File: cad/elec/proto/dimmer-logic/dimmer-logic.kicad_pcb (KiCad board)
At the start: 2 copper layers, 41 parts, among them P1 AC_IN, P2 DC_OUT, P3 LOGIC_OUT, P4 I2C_BUS, P5 dsPIC_PGM, U1 7805, U2 LTC6253, U3 TCA9406, U4 dsPIC33FJ06GS101A, U5 74LS08, U6 74LS32, U7 MIC52393.3-YS, X1 10 MHz

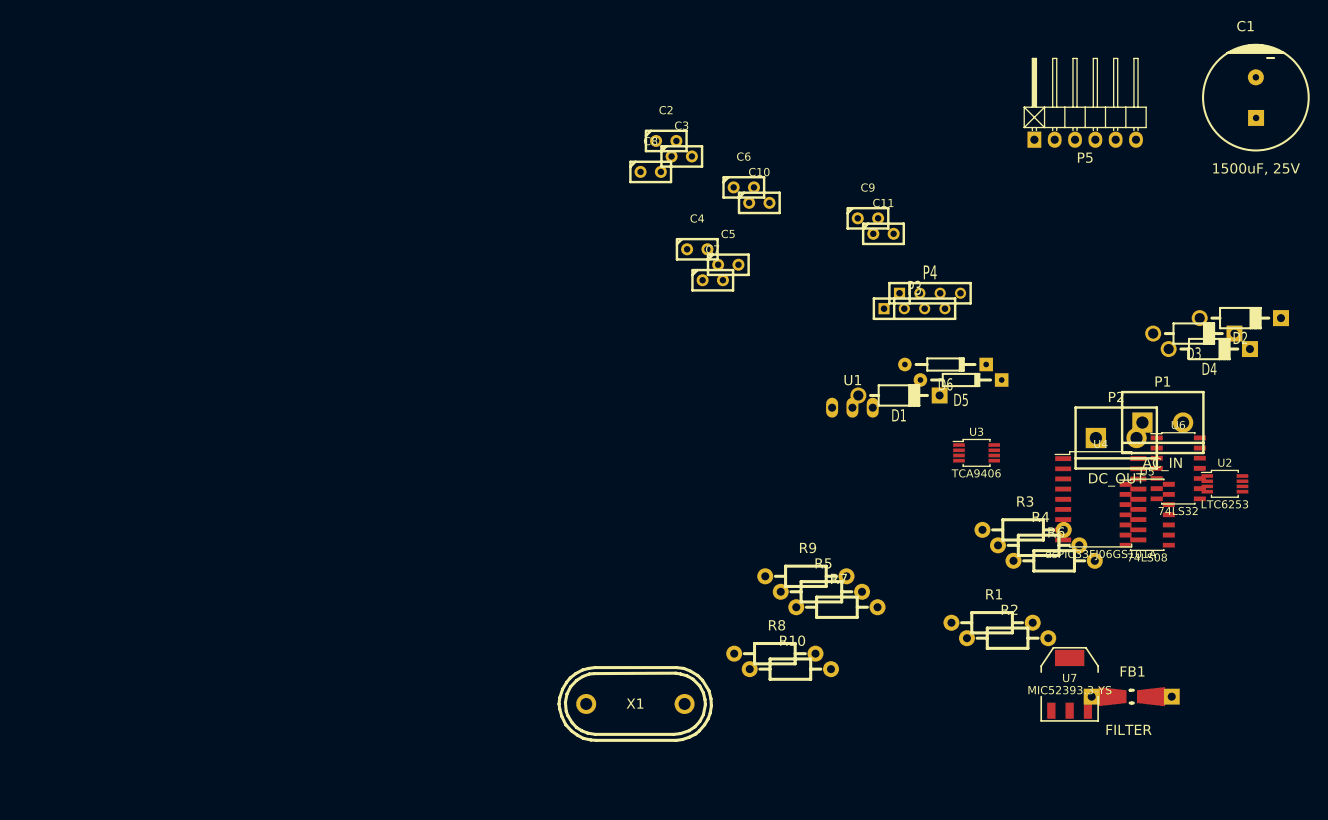
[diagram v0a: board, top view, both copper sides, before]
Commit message: Adds a first prototype layout for dimmer-logic
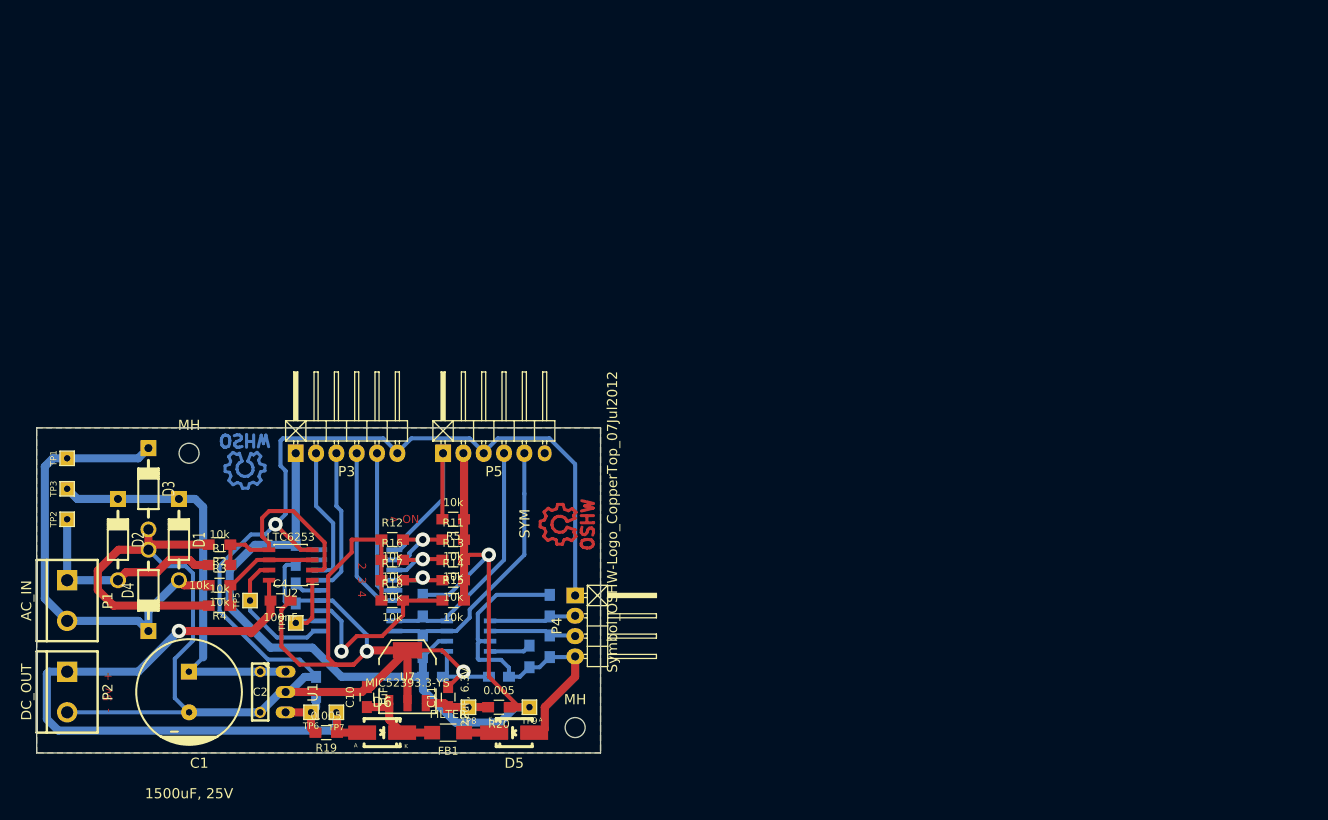
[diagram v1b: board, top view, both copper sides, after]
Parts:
- removed C5: 20pF, Capacitors_ThroughHole:Capacitor3MMDiscRM2.5
- removed U5: 74LS08, Housings_SOIC:SOIC-14_3.9x8.7mm_Pitch1.27mm
- removed U6: 74LS32, Housings_SOIC:SOIC-14_3.9x8.7mm_Pitch1.27mm
- removed X1: 10 MHz, Crystals:Crystal_HC48-U_Vertical
- added MH: MountingHole_2-5mm_RevA_Date21Jun2010, Mounting_Holes:MountingHole_2-5mm, F.Cu at (92.7, 73.7)
- added MH: MountingHole_2-5mm_RevA_Date21Jun2010, Mounting_Holes:MountingHole_2-5mm, F.Cu at (141.0, 108.0)
- added R11: 10k, Resistors_SMD:R_0805_HandSoldering, F.Cu at (125.7, 84.5)
- added R12: 10k, Resistors_SMD:R_0805_HandSoldering, F.Cu at (118.1, 84.5)
- added R13: 10k, Resistors_SMD:R_0805_HandSoldering, F.Cu at (125.7, 87.0)
- added R14: 10k, Resistors_SMD:R_0805_HandSoldering, F.Cu at (125.7, 89.5)
- added R15: 10k, Resistors_SMD:R_0805_HandSoldering, F.Cu at (125.7, 92.1)
- added R16: 10k, Resistors_SMD:R_0805_HandSoldering, F.Cu at (118.1, 87.0)
- added R17: 10k, Resistors_SMD:R_0805_HandSoldering, F.Cu at (118.1, 89.5)
- added R18: 10k, Resistors_SMD:R_0805_HandSoldering, F.Cu at (118.1, 92.1)
- added R19: 0.005, Resistors_SMD:R_0805_HandSoldering, F.Cu at (109.9, 108.6)
- added R20: 0.005, Resistors_SMD:R_0805_HandSoldering, F.Cu at (131.4, 105.4)
- added SYM: Symbol_OSHW-Logo_CopperTop_07Jul2012, Symbols:Symbol_OSHW-Logo_CopperTop, B.Cu at (99.7, 75.6)
- added SYM: Symbol_OSHW-Logo_CopperTop_07Jul2012, Symbols:Symbol_OSHW-Logo_CopperTop, F.Cu at (139.1, 82.5)
- added TP1: L, Connect:SIL-1, F.Cu at (77.5, 74.3)
- added TP2: N, Connect:SIL-1, F.Cu at (77.5, 81.9)
- added TP3: RED, Connect:SIL-1, F.Cu at (77.5, 78.1)
- added TP4: DET_L, Connect:SIL-1, F.Cu at (106.0, 94.9)
- added TP5: DET_N, Connect:SIL-1, F.Cu at (100.3, 92.1)
- added TP6: 5VA, Connect:SIL-1, F.Cu at (108.0, 106.0)
- added TP7: 5VB, Connect:SIL-1, F.Cu at (111.1, 106.0)
- added TP8: 3v3A, Connect:SIL-1, F.Cu at (127.6, 105.4)
- added TP9: 3v3B, Connect:SIL-1, F.Cu at (135.3, 105.4)
- C10, C11: footprint Capacitors_ThroughHole:Capacitor3MMDiscRM2.5 -> Capacitors_SMD:C_0805_HandSoldering
- C2: footprint Capacitors_ThroughHole:Capacitor3MMDiscRM2.5 -> Discret:C2
- C3, C6, C7, C8, C9: footprint Capacitors_ThroughHole:Capacitor3MMDiscRM2.5 -> Capacitors_SMD:C_0805_HandSoldering; moved to B.Cu
- C4: value 20pF -> 100nF; footprint Capacitors_ThroughHole:Capacitor3MMDiscRM2.5 -> Capacitors_SMD:C_0805_HandSoldering
- D5, D6: footprint Diodes_ThroughHole:Diode_DO-35_SOD27_Horizontal_RM10 -> Diodes_SMD:Diode-SMA_Handsoldering
- FB1: footprint Resistors_Universal:Resistor_SMD+THTuniversal_0805to1206_RM10_HandSoldering -> Resistors_SMD:R_1206_HandSoldering
- P3: footprint Connect:SIL-4 -> Pin_Headers:Pin_Header_Angled_1x06
- P4: footprint Connect:SIL-4 -> Pin_Headers:Pin_Header_Angled_1x04
- R1, R2, R3, R4, R5: footprint Resistors_ThroughHole:Resistor_Horizontal_RM10mm -> Resistors_SMD:R_0805_HandSoldering
- R10, R6, R7, R8, R9: footprint Resistors_ThroughHole:Resistor_Horizontal_RM10mm -> Resistors_SMD:R_0805_HandSoldering; moved to B.Cu
- U1: value 7805 -> LM7805CT
- U2: footprint Housings_SSOP:MSOP-8_3x3mm_Pitch0.65mm -> Housings_SOIC:SOIC-8_3.9x4.9mm_Pitch1.27mm
- U3: value TCA9406 -> PCA9306D; footprint Housings_SSOP:MSOP-8_3x3mm_Pitch0.65mm -> Housings_SOIC:SOIC-8_3.9x4.9mm_Pitch1.27mm; moved to B.Cu
- U4: moved to B.Cu
- moved C1 152.6 mm to (92.7, 103.5), turned to 180 degrees
- moved D2 143.0 mm to (83.8, 84.5), turned to 90 degrees
- moved P1 138.7 mm to (77.5, 92.1), turned to 270 degrees
- moved D4 136.0 mm to (87.6, 90.8), turned to 270 degrees
- moved P2 134.9 mm to (77.5, 103.5), turned to 270 degrees
- moved D3 132.1 mm to (87.6, 78.1), turned to 90 degrees
- moved U2 117.2 mm to (105.4, 87.6), turned to 180 degrees
- moved R4 102.7 mm to (96.5, 92.7), turned to 180 degrees
- moved R3 100.7 mm to (96.5, 90.2)
- moved R2 99.2 mm to (96.5, 85.1), turned to 180 degrees
- moved R1 96.8 mm to (96.5, 87.6)
- moved U4 93.7 mm to (113.7, 90.8), turned to 180 degrees
- moved D1 91.8 mm to (91.4, 84.5), turned to 90 degrees
- moved FB1 85.6 mm to (125.1, 108.6), turned to 180 degrees
- moved C2 85.6 mm to (101.6, 103.5), turned to 270 degrees
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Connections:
- net Net-(R3-Pad2) renamed /ac_dc_supply/l_low
- C1 pad 1: Net-(C1-Pad1) -> /ac_dc_supply/IN_RED
- C11 pad 1: +3.3V -> Net-(C11-Pad1)
- C2 pad 1: Net-(C1-Pad1) -> /ac_dc_supply/IN_RED
- C3 pad 1: Net-(C3-Pad1) -> /ac_dc_supply/LM_OUT
- C4 pad 1: Net-(C4-Pad1) -> +5V
- C6 pad 1: GND -> /dsPIC/5V_BUS
- C6 pad 2: /dsPIC/5V_BUS -> GND
- D1 pad 1: Net-(D1-Pad1) -> /ac_dc_supply/l_in
- D1 pad 2: Net-(C1-Pad1) -> /ac_dc_supply/IN_RED
- D2 pad 1: Net-(D2-Pad1) -> /ac_dc_supply/n_in
- D2 pad 2: Net-(C1-Pad1) -> /ac_dc_supply/IN_RED
- D3 pad 2: Net-(D1-Pad1) -> /ac_dc_supply/l_in
- D4 pad 2: Net-(D4-Pad2) -> /ac_dc_supply/l_in
- P3 pad 1: /dsPIC/nh -> +3.3V
- P3 pad 2: /dsPIC/nl -> /dsPIC/ll
- P3 pad 4: /dsPIC/ll -> /dsPIC/nh
- P4 pad 2: /dsPIC/SCL_BUS -> /dsPIC/SDA_BUS
- P4 pad 3: /dsPIC/SDA_BUS -> /dsPIC/SCL_BUS
- P5 pad 4: /dsPIC/PGD -> /dsPIC/SDA_UC
- P5 pad 5: /dsPIC/PGC -> /dsPIC/SCL_UC
- R1 pad 1: Net-(D2-Pad1) -> /ac_dc_supply/n_in
- R1 pad 2: Net-(R1-Pad2) -> /ac_dc_supply/n_low
- R10 pad 1: Net-(R10-Pad1) -> /dsPIC/5V_BUS
- R10 pad 2: /dsPIC/5V_BUS -> Net-(R10-Pad2)
- R2 pad 1: Net-(R1-Pad2) -> /ac_dc_supply/n_low
- R3 pad 1: Net-(D1-Pad1) -> /ac_dc_supply/l_in
- R6 pad 1: /dsPIC/5V_BUS -> /dsPIC/SDA_BUS
- R6 pad 2: Net-(R6-Pad2) -> /dsPIC/5V_BUS
- R7 pad 1: +3.3V -> /dsPIC/SDA_UC
- R7 pad 2: /dsPIC/SCL_UC -> +3.3V
- R8 pad 1: GND -> /dsPIC/SCL_BUS
- R8 pad 2: /dsPIC/I2C_EN -> /dsPIC/5V_BUS
- R9 pad 1: /dsPIC/SDA_UC -> /dsPIC/SCL_UC
- U1 pad 1: (no net) -> /ac_dc_supply/IN_RED
- U1 pad 2: (no net) -> GND
- U1 pad 3: (no net) -> /ac_dc_supply/LM_OUT
- U2 pad 2: Net-(U2-Pad2) -> /ac_dc_supply/n_low
- U2 pad 5: Net-(U2-Pad2) -> /ac_dc_supply/n_low
- U2 pad 7: /ac_dc_supply/phase_- -> /dsPIC/ac_phase_-
- U3 pad 1: /dsPIC/SDA_BUS -> GND
- U3 pad 2: GND -> +3.3V
- U3 pad 3: +3.3V -> /dsPIC/SCL_UC
- U3 pad 5: /dsPIC/SCL_UC -> /dsPIC/SDA_BUS
- U3 pad 6: /dsPIC/I2C_EN -> /dsPIC/SCL_BUS
- U3 pad 8: /dsPIC/SCL_BUS -> Net-(R10-Pad2)
- U4 pad 10: Net-(U4-Pad10) -> /dsPIC/ac_phase_-
- U4 pad 11: /dsPIC/PGD -> /dsPIC/ac_phase_+
- U4 pad 12: /dsPIC/PGC -> /dsPIC/ADDR4
- U4 pad 15: Net-(U4-Pad15) -> /dsPIC/lh
- U4 pad 16: Net-(U4-Pad16) -> /dsPIC/ll
- U4 pad 2: Net-(U4-Pad2) -> /dsPIC/ADDR1
- U4 pad 3: Net-(U4-Pad3) -> /dsPIC/ADDR2
- U4 pad 4: Net-(U4-Pad4) -> /dsPIC/ADDR3
- U4 pad 5: /dsPIC/I2C_EN -> /dsPIC/nl
- U4 pad 6: Net-(C4-Pad1) -> /dsPIC/nh
- U4 pad 7: Net-(C5-Pad1) -> /dsPIC/I2C_EN
- U7 pad 3: +3.3V -> Net-(C11-Pad1)
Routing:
- net GND: track 0.00 -> 323.7 mm, vias 0 -> 3
- net +3.3V: track 0.00 -> 137.0 mm, vias 0 -> 1
- net +5V: track 0.00 -> 85.7 mm, vias 0 -> 1
- net /ac_dc_supply/l_in: track 0.00 -> 57.0 mm
- net /ac_dc_supply/IN_RED: track 0.00 -> 51.4 mm
- net /dsPIC/5V_BUS: track 0.00 -> 44.5 mm
- net /dsPIC/SCL_UC: track 0.00 -> 34.0 mm
- net /dsPIC/SDA_UC: track 0.00 -> 31.4 mm
- net /ac_dc_supply/n_in: track 0.00 -> 26.6 mm
- net /ac_dc_supply/n_low: track 0.00 -> 26.6 mm
- net /dsPIC/ADDR4: track 0.00 -> 23.5 mm, vias 0 -> 1
- net /dsPIC/~MCLR: track 0.00 -> 23.4 mm
- net /dsPIC/nh: track 0.00 -> 21.3 mm
- net /dsPIC/nl: track 0.00 -> 18.9 mm
- net /dsPIC/lh: track 0.00 -> 18.3 mm
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- added copper zone on B.Cu, net GND
- added copper zone on F.Cu, net GND
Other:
- board outline added: 70.5 x 40.6 mm
- net class Default: clearance 0.254 -> 0.508; trace_width 0.254 -> 0.508; via_dia 0.889 -> 1.8; via_drill 0.635 -> 0.9
- net class power added: clearance 0.508, trace_width 1.016, via_dia 2, via_drill 1
- rule trace_clearance: 0.254 -> 0.508
- rule trace_min: 0.254 -> 0.508
- rule via_min_size: 0.889 -> 0.9
- board text added: "- 5v +"
- board text added: "-> ON"
- board text added: "2 3 4"
